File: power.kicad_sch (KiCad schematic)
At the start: 57 parts, among them J4 Conn_01x02, J5 Conn_01x02, J6 Conn_01x02, Q29 AO3401, Q30 Q_NPN_BEC, T1 COMMON_MODE_CHOKE, U14 NCP1117ST33, U19 TPS54428DDA, U2 TPS54202

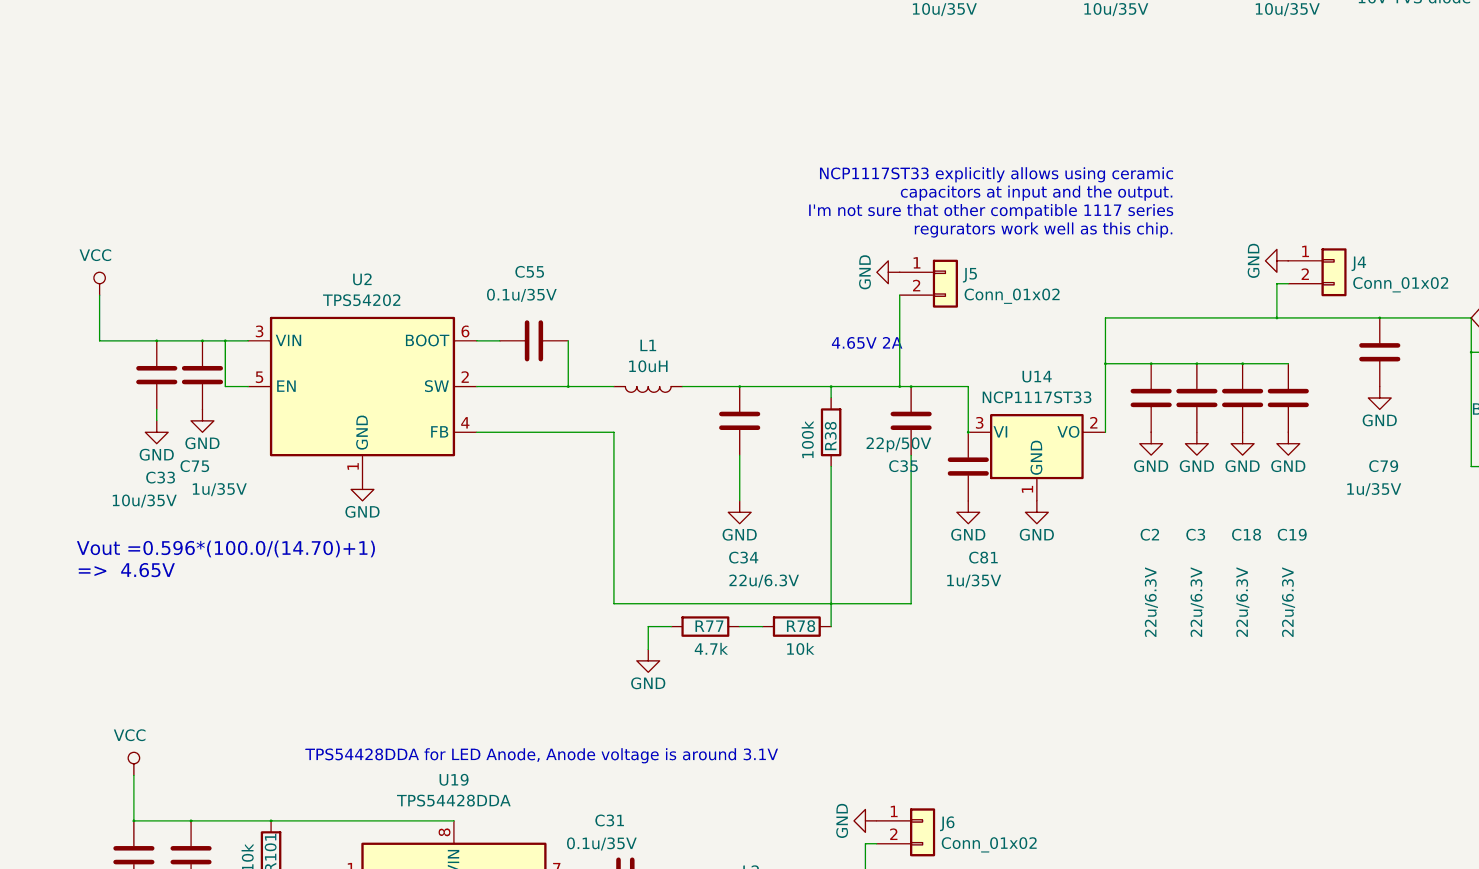
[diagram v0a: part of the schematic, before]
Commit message: Changed LDO to one which has more lower drop voltage; DRC clear
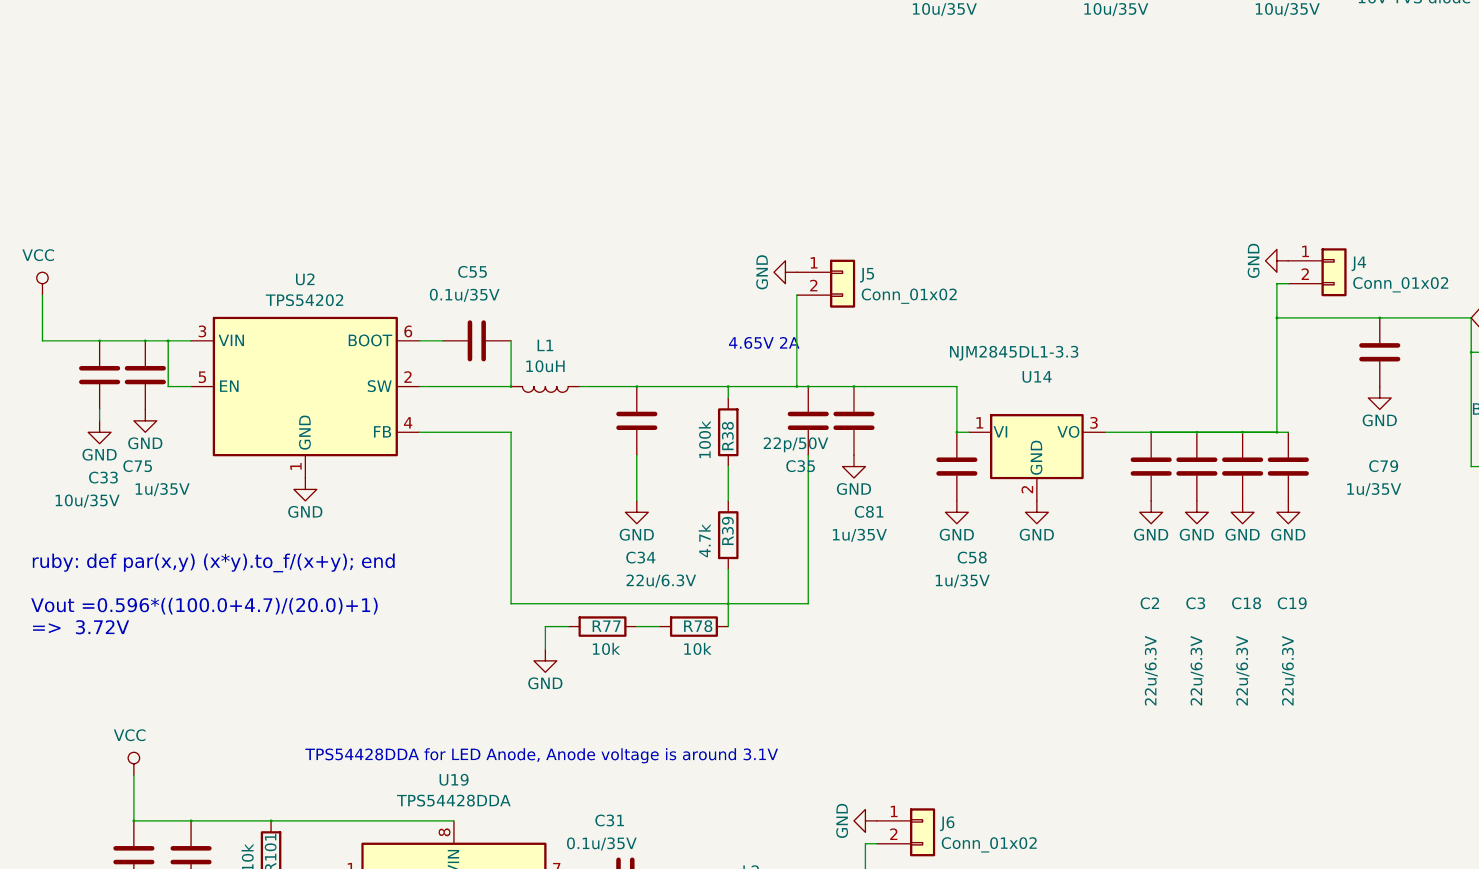
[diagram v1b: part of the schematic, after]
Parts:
- removed U14: NCP1117ST33, Package_TO_SOT_SMD:SOT-223-3_TabPin2, symbol regul:AP1117-33
- added C58: 1u/35V, Capacitor_SMD:C_0603_1608Metric_Pad1.05x0.95mm_HandSolder, symbol dotmatrix_64x48-rescue:C-device
- added R39: 4.7k, Resistor_SMD:R_0603_1608Metric_Pad1.05x0.95mm_HandSolder, symbol dotmatrix_64x48-rescue:R-device
- added U14: NJM2845DL1-3.3, Package_TO_SOT_SMD:TO-252-3_TabPin2, symbol regul:LF33_TO252
- R77: value 4.7k -> 10k
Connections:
- net GND: now also C58.2, U14.2 (GND)
- net LEDLOGICVDD: now also U14.3 (VO)
- net at C34.1, C35.1, C81.1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: now also C58.1, U14.1 (VI)
- net at C35.2, R78.1, U2.4 (FB): now also R39.2; no longer R38.1
- new net: R38.1, R39.1
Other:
- note added: "ruby: def par(x,y) (x*y).to_f/(x+y); end Vout =0.596*((100.0+4.7)/(20.0)+1) => 3.72V"
- note removed: "NCP1117ST33 explicitly allows using ceramic capacitors at input and the output. I'm not sure that other compatible 1117 series regurators work well as this chip."
- note removed: "Vout =0.596*(100.0/(14.70)+1) => 4.65V"
- moved on the sheet: C18, C19, C2, C3, C33, C34, C35, C55, C75, C81, J5, L1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

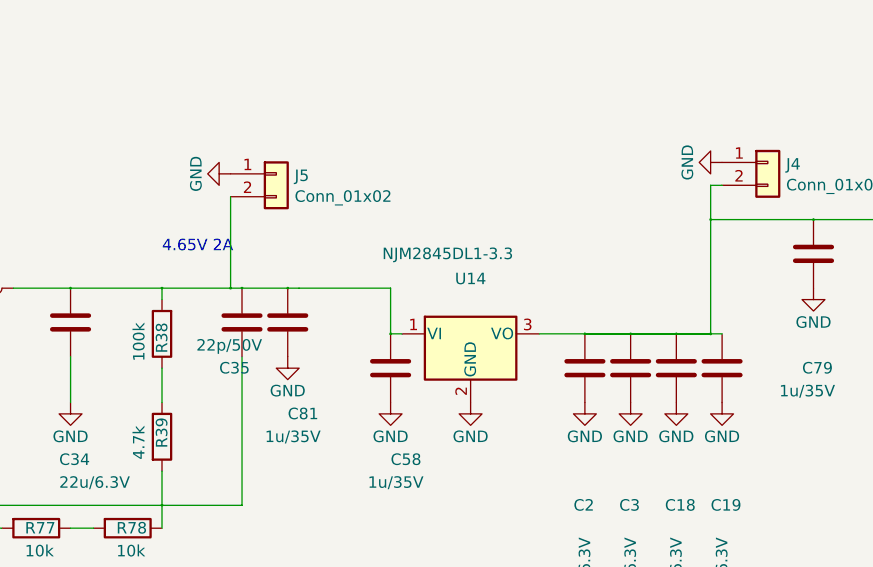
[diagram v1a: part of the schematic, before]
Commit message: Fixed a comment mismatch; Why KiCAD changes more files than I edited ...
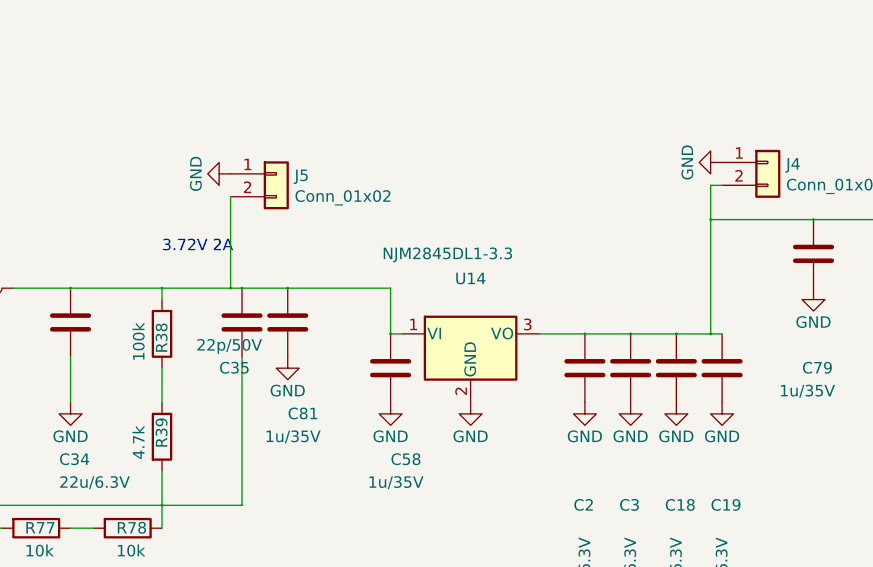
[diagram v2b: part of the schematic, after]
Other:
- note added: "3.72V 2A"
- note removed: "4.65V 2A"
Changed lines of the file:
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@@
     (stroke (width 0) (type solid) (color 0 0 0 0))
   )
-  (wire (pts (xy 106.68 86.36) (xy 105.41 86.36))
-    (stroke (width 0) (type solid) (color 0 0 0 0))
-  )
-  (wire (pts (xy 106.68 86.36) (xy 116.84 86.36))
+  (wire (pts (xy 105.41 86.36) (xy 116.84 86.36))
     (stroke (width 0) (type solid) (color 0 0 0 0))
   )
@@
     (stroke (width 0) (type solid) (color 0 0 0 0))
   )
-  (wire (pts (xy 143.51 91.44) (xy 138.43 91.44))
-    (stroke (width 0) (type solid) (color 0 0 0 0))
-  )
   (wire (pts (xy 143.51 91.44) (xy 148.59 91.44))
     (stroke (width 0) (type solid) (color 0 0 0 0))
@@
     (stroke (width 0) (type solid) (color 0 0 0 0))
   )
-  (wire (pts (xy 148.59 91.44) (xy 143.51 91.44))
-    (stroke (width 0) (type solid) (color 0 0 0 0))
-  )
   (wire (pts (xy 151.13 26.67) (xy 151.13 27.94))
     (stroke (width 0) (type solid) (color 0 0 0 0))
@@
   )
   (wire (pts (xy 152.4 78.74) (xy 163.83 78.74))
-    (stroke (width 0) (type solid) (color 0 0 0 0))
-  )
-  (wire (pts (xy 152.4 91.44) (xy 148.59 91.44))
     (stroke (width 0) (type solid) (color 0 0 0 0))
   )
@@
     (effects (font (size 1.27 1.27)) (justify right bottom))
   )
-  (text "4.65V 2A" (at 91.44 82.55 0)
+  (text "3.72V 2A" (at 91.44 82.55 0)
     (effects (font (size 1.27 1.27)) (justify left bottom))
   )

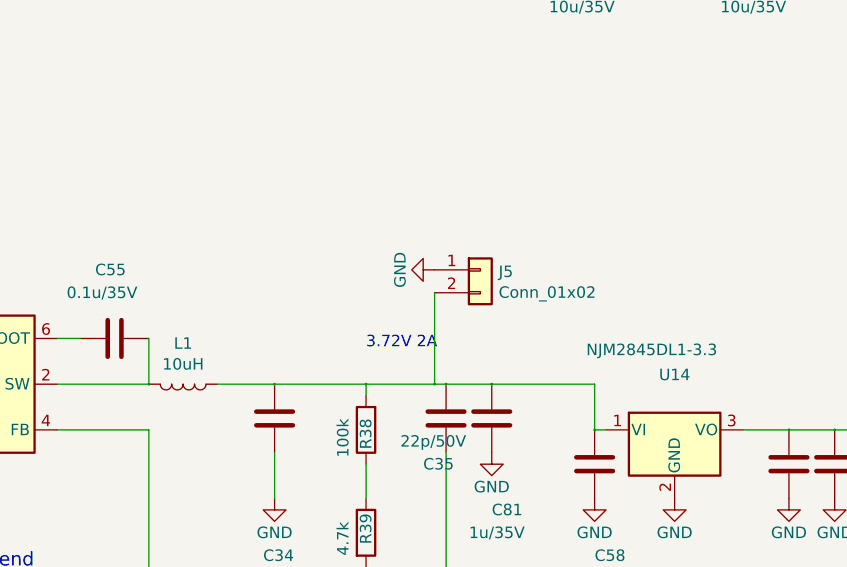
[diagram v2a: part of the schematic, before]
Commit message: To use WS2812-2020 as status LEDs; No critical DRC errors found
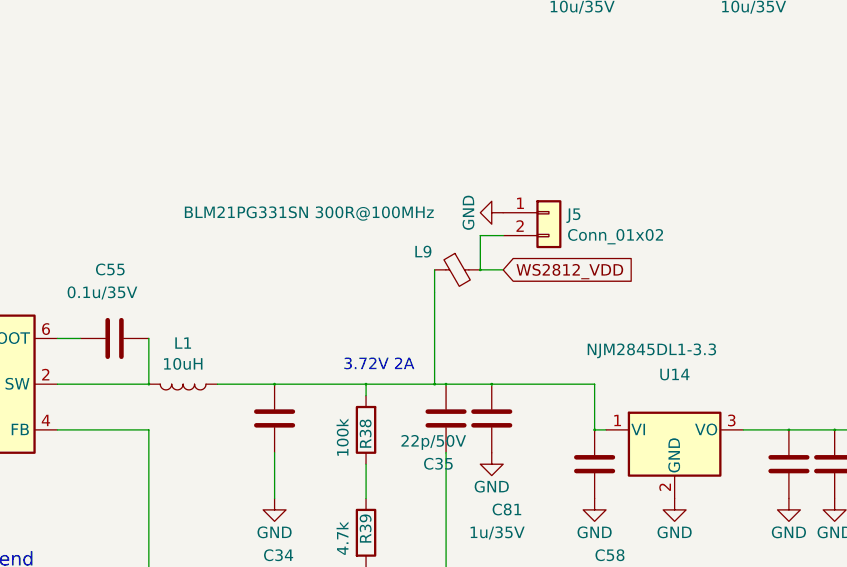
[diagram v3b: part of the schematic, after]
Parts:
- added L9: BLM21PG331SN 300R@100MHz, Capacitor_SMD:C_0805_2012Metric_Pad1.18x1.45mm_HandSolder, symbol dotmatrix_64x48-rescue:Ferrite_Bead_Small-device
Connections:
- net at C34.1, C35.1, C58.1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: now also L9.1; no longer J5.2 (Pin_2)
- new net WS2812_VDD: J5.2 (Pin_2), L9.2
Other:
- moved on the sheet: J5
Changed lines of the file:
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@@
   (junction (at 100.33 86.36) (diameter 0.3048) (color 0 0 0 0))
   (junction (at 101.6 144.78) (diameter 0.3048) (color 0 0 0 0))
+  (junction (at 104.14 73.66) (diameter 0.3048) (color 0 0 0 0))
   (junction (at 105.41 86.36) (diameter 0.3048) (color 0 0 0 0))
   (junction (at 106.68 144.78) (diameter 0.3048) (color 0 0 0 0))
@@
     (stroke (width 0) (type solid) (color 0 0 0 0))
   )
+  (wire (pts (xy 99.06 73.66) (xy 99.06 76.2))
+    (stroke (width 0) (type solid) (color 0 0 0 0))
+  )
   (wire (pts (xy 99.06 76.2) (xy 99.06 86.36))
     (stroke (width 0) (type solid) (color 0 0 0 0))
@@
     (stroke (width 0) (type solid) (color 0 0 0 0))
   )
+  (wire (pts (xy 104.14 69.85) (xy 104.14 73.66))
+    (stroke (width 0) (type solid) (color 0 0 0 0))
+  )
+  (wire (pts (xy 104.14 73.66) (xy 106.68 73.66))
+    (stroke (width 0) (type solid) (color 0 0 0 0))
+  )
   (wire (pts (xy 105.41 86.36) (xy 100.33 86.36))
     (stroke (width 0) (type solid) (color 0 0 0 0))
   )
   (wire (pts (xy 105.41 86.36) (xy 116.84 86.36))
+    (stroke (width 0) (type solid) (color 0 0 0 0))
+  )
+  (wire (pts (xy 106.68 69.85) (xy 104.14 69.85))
     (stroke (width 0) (type solid) (color 0 0 0 0))
   )
@@
     (effects (font (size 1.27 1.27)) (justify right bottom))
   )
-  (text "3.72V 2A" (at 91.44 82.55 0)
+  (text "3.72V 2A" (at 88.9 85.09 0)
     (effects (font (size 1.27 1.27)) (justify left bottom))
   )
@@
     (effects (font (size 1.524 1.524)) (justify left))
   )
+  (global_label "WS2812_VDD" (shape input) (at 106.68 73.66 0)
+    (effects (font (size 1.27 1.27)) (justify left))
+  )
   (global_label "LEDVDD" (shape input) (at 127 144.78 0)
     (effects (font (size 1.524 1.524)) (justify left))
@@
     (property "Datasheet" "" (id 3) (at 97.79 31.75 0))
   )
-  (symbol (lib_id "dotmatrix_64x48-rescue:GND-power") (at 99.06 73.66 270) (mirror x) (unit 1)
-    (in_bom yes) (on_board yes)
-    (property "Reference" "#PWR03" (id 0) (at 92.71 73.66 0)
-      (effects (font (size 1.27 1.27)) hide)
-    )
-    (property "Value" "GND" (id 1) (at 95.25 73.66 0))
-    (property "Footprint" "" (id 2) (at 99.06 73.66 0))
-    (property "Datasheet" "" (id 3) (at 99.06 73.66 0))
-  )
   (symbol (lib_id "dotmatrix_64x48-rescue:GND-power") (at 105.41 93.98 0) (mirror y) (unit 1)
     (in_bom yes) (on_board yes)
@@
     (property "Datasheet" "" (id 3) (at 105.41 93.98 0))
   )
+  (symbol (lib_id "dotmatrix_64x48-rescue:GND-power") (at 106.68 67.31 270) (mirror x) (unit 1)
+    (in_bom yes) (on_board yes)
+    (property "Reference" "#PWR03" (id 0) (at 100.33 67.31 0)
+      (effects (font (size 1.27 1.27)) hide)
+    )
+    (property "Value" "GND" (id 1) (at 102.87 67.31 0))
+    (property "Footprint" "" (id 2) (at 106.68 67.31 0))
+    (property "Datasheet" "" (id 3) (at 106.68 67.31 0))
+  )
   (symbol (lib_id "dotmatrix_64x48-rescue:GND-power") (at 107.95 134.62 270) (mirror x) (unit 1)
     (in_bom yes) (on_board yes)
@@
     (property "Datasheet" "" (id 3) (at 267.97 92.71 0))
   )
+  (symbol (lib_id "dotmatrix_64x48-rescue:Ferrite_Bead_Small-device") (at 101.6 73.66 90) (mirror x) (unit 1)
+    (in_bom yes) (on_board yes)
+    (property "Reference" "L9" (id 0) (at 97.79 71.6788 90))
+    (property "Value" "BLM21PG331SN 300R@100MHz" (id 1) (at 85.09 67.31 90))
+    (property "Footprint" "Capacitor_SMD:C_0805_2012Metric_Pad1.18x1.45mm_HandSolder" (id 2) (at 101.6 73.66 0)
+      (effects (font (size 1.27 1.27)) hide)
+    )
+    (property "Datasheet" "" (id 3) (at 101.6 73.66 0))
+  )
   (symbol (lib_id "dotmatrix_64x48-rescue:Ferrite_Bead_Small-device") (at 179.07 95.25 90) (mirror x) (unit 1)
     (in_bom yes) (on_board yes)
@@
     (property "Datasheet" "" (id 3) (at 179.07 95.25 0))
   )
-  (symbol (lib_id "Connector_Generic:Conn_01x02") (at 104.14 73.66 0) (unit 1)
-    (in_bom yes) (on_board yes)
-    (property "Reference" "J5" (id 0) (at 106.172 73.8632 0)
-      (effects (font (size 1.27 1.27)) (justify left))
-    )
-    (property "Value" "Conn_01x02" (id 1) (at 106.172 76.1746 0)
-      (effects (font (size 1.27 1.27)) (justify left))
-    )
-    (property "Footprint" "Connector_PinHeader_2.54mm:PinHeader_1x02_P2.54mm_Vertical" (id 2) (at 104.14 73.66 0)
-      (effects (font (size 1.27 1.27)) hide)
-    )
-    (property "Datasheet" "~" (id 3) (at 104.14 73.66 0)
-      (effects (font (size 1.27 1.27)) hide)
-    )
+  (symbol (lib_id "Connector_Generic:Conn_01x02") (at 111.76 67.31 0) (unit 1)
+    (in_bom yes) (on_board yes)
+    (property "Reference" "J5" (id 0) (at 113.792 67.5132 0)
+      (effects (font (size 1.27 1.27)) (justify left))
+    )
+    (property "Value" "Conn_01x02" (id 1) (at 113.792 69.8246 0)
+      (effects (font (size 1.27 1.27)) (justify left))
+    )
+    (property "Footprint" "Connector_PinHeader_2.54mm:PinHeader_1x02_P2.54mm_Vertical" (id 2) (at 111.76 67.31 0)
+      (effects (font (size 1.27 1.27)) hide)
+    )
+    (property "Datasheet" "~" (id 3) (at 111.76 67.31 0)
+      (effects (font (size 1.27 1.27)) hide)
+    )

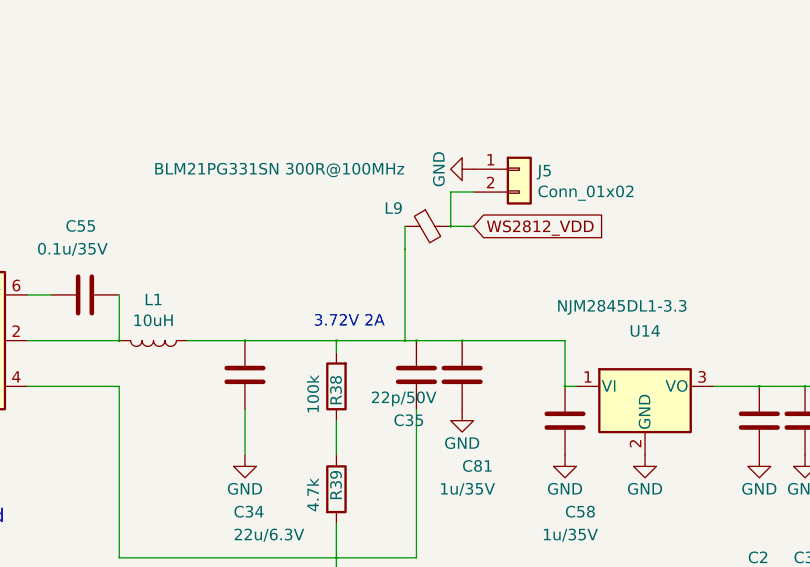
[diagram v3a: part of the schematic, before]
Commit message: Routing adjustments; DRC should be ok
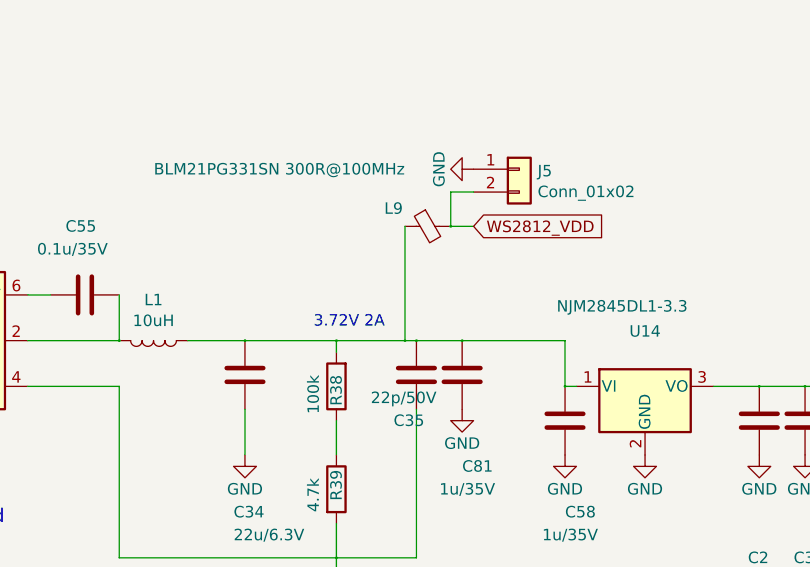
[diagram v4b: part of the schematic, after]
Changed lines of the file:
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@@
-(kicad_sch (version 20200828) (generator eeschema)
-  (page 9 10)
+(kicad_sch (version 20201015) (generator eeschema)
+  (page 1 10)
   (paper "A4")
   (junction (at 21.59 81.28) (diameter 0.3048) (color 0 0 0 0))
@@
     (stroke (width 0) (type solid) (color 0 0 0 0))
   )
-  (wire (pts (xy 99.06 73.66) (xy 99.06 76.2))
-    (stroke (width 0) (type solid) (color 0 0 0 0))
-  )
-  (wire (pts (xy 99.06 76.2) (xy 99.06 86.36))
-    (stroke (width 0) (type solid) (color 0 0 0 0))
-  )
+  (wire (pts (xy 99.06 73.66) (xy 99.06 86.36))
+    (stroke (width 0) (type solid) (color 0 0 0 0))
+  )
